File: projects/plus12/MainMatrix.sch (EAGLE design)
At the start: 41 parts, among them SW1 RSTSWSMD, SW2 TRANSFERPADDY

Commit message: Getting ready for pictures
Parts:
- INT1: value INTRCNNT -> INTRCNNT4X2; device Keys:INTRCNNT -> Keys:INTRCNNT4X2
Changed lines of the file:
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@@
 <part name="SW2" library="Keys" library_urn="urn:adsk.eagle:library:1331239" deviceset="TRANSFER" device="PADDY" package3d_urn="urn:adsk.eagle:package:3624143/2"/>
 <part name="JK1" library="Keys" library_urn="urn:adsk.eagle:library:1331239" deviceset="TRRSJACK" device="" package3d_urn="urn:adsk.eagle:package:1393948/13"/>
-<part name="INT1" library="Keys" library_urn="urn:adsk.eagle:library:1331239" deviceset="INTRCNNT" device="" package3d_urn="urn:adsk.eagle:package:3650901/1"/>
+<part name="INT1" library="Keys" library_urn="urn:adsk.eagle:library:1331239" deviceset="INTRCNNT" device="4X2"/>
 </parts>
 <sheets>

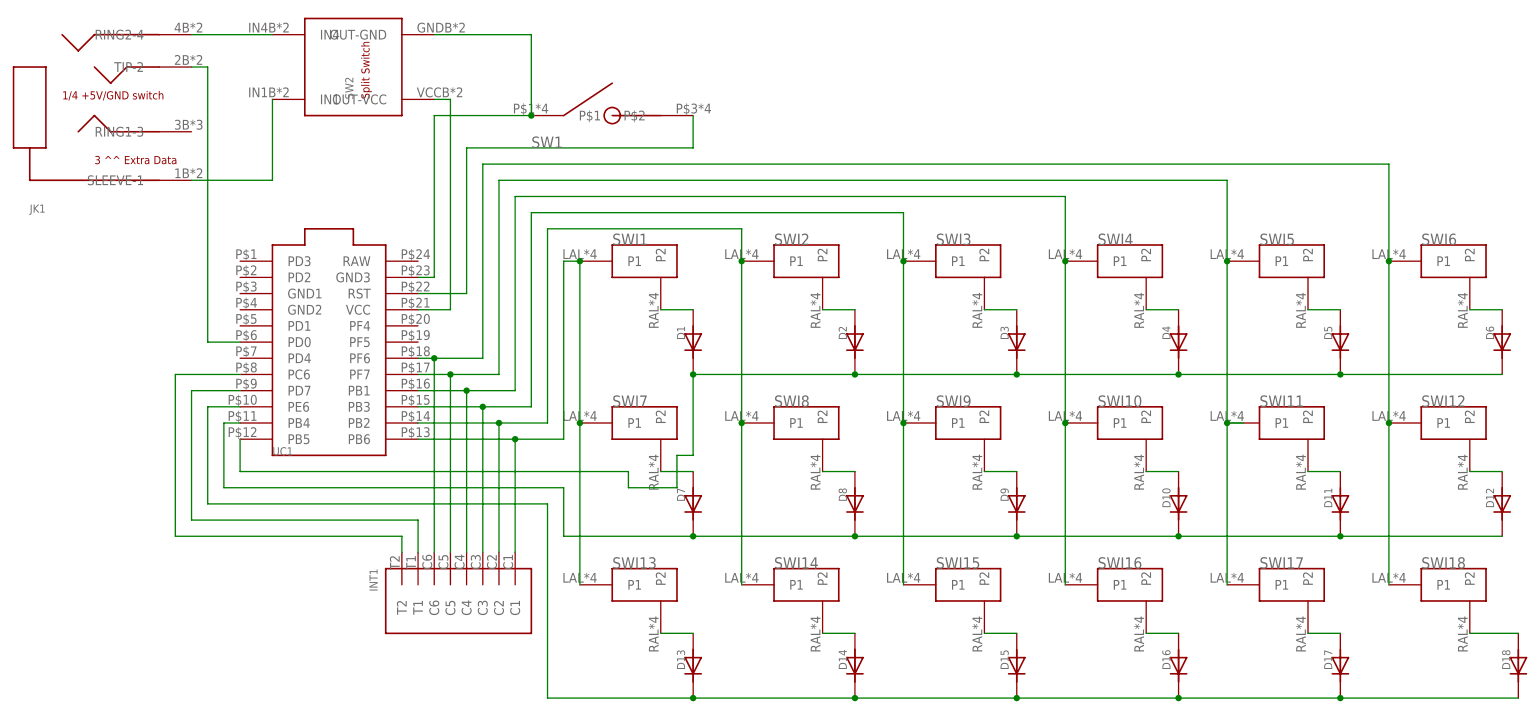
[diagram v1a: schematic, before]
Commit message: Adding low profile support
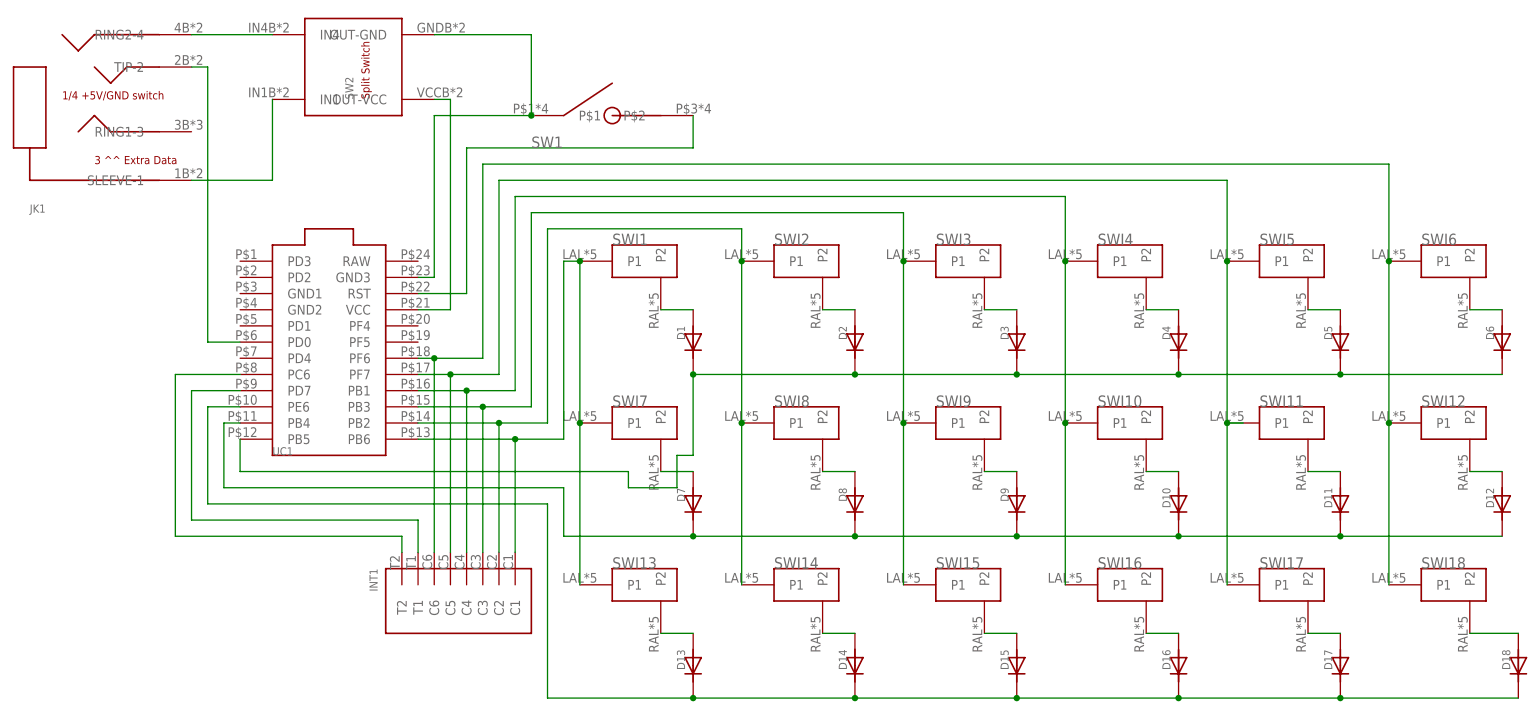
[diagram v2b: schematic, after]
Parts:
- JK1: value TRRSJACK -> TRRSJACKUNDER; device Keys:TRRSJACK -> Keys:TRRSJACKUNDER
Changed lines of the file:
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@@
 <part name="D17" library="Keys" library_urn="urn:adsk.eagle:library:1331239" deviceset="DIODE" device="" package3d_urn="urn:adsk.eagle:package:3624144/3"/>
 <part name="D18" library="Keys" library_urn="urn:adsk.eagle:library:1331239" deviceset="DIODE" device="" package3d_urn="urn:adsk.eagle:package:3624144/3"/>
-<part name="UC1" library="Keys" library_urn="urn:adsk.eagle:library:1331239" deviceset="PROMICRO" device="UNDER" package3d_urn="urn:adsk.eagle:package:1399517/9"/>
+<part name="UC1" library="Keys" library_urn="urn:adsk.eagle:library:1331239" deviceset="PROMICRO" device="UNDER" package3d_urn="urn:adsk.eagle:package:1399517/10"/>
 <part name="SW1" library="Keys" library_urn="urn:adsk.eagle:library:1331239" deviceset="RSTSW" device="SMD" package3d_urn="urn:adsk.eagle:package:1393947/7"/>
 <part name="SW2" library="Keys" library_urn="urn:adsk.eagle:library:1331239" deviceset="TRANSFER" device="PADDY" package3d_urn="urn:adsk.eagle:package:3624143/2"/>
-<part name="JK1" library="Keys" library_urn="urn:adsk.eagle:library:1331239" deviceset="TRRSJACK" device="" package3d_urn="urn:adsk.eagle:package:1393948/13"/>
+<part name="JK1" library="Keys" library_urn="urn:adsk.eagle:library:1331239" deviceset="TRRSJACK" device="UNDER" package3d_urn="urn:adsk.eagle:package:1393948/13"/>
 <part name="INT1" library="Keys" library_urn="urn:adsk.eagle:library:1331239" deviceset="INTRCNNT" device="4X2"/>
 </parts>

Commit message: more updates than should be in one commit, lots of work
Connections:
- new net N$36: JK1.EDATA, JK1.RING1-3
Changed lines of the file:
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@@
 <?xml version="1.0" encoding="utf-8"?>
 <!DOCTYPE eagle SYSTEM "eagle.dtd">
-<eagle version="9.1.0">
+<eagle version="9.1.1">
 <drawing>
 <settings>
@@
 </segment>
 </net>
+<net name="N$36" class="0">
+<segment>
+<pinref part="JK1" gate="G$1" pin="RING1-3"/>
+<wire x1="-60.96" y1="96.52" x2="-53.34" y2="96.52" width="0.1524" layer="91"/>
+<wire x1="-53.34" y1="96.52" x2="-53.34" y2="83.82" width="0.1524" layer="91"/>
+<pinref part="JK1" gate="G$1" pin="EDATA"/>
+<wire x1="-53.34" y1="83.82" x2="-60.96" y2="83.82" width="0.1524" layer="91"/>
+</segment>
+</net>
